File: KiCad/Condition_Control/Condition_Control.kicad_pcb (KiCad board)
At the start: 2 copper layers, 100 x 100 mm, 16 parts, among them J1 Conn_01x04_Socket, J2 Conn_01x03_Socket, J3 Conn_01x02_Socket, J4 Conn_01x02_Socket, U1 74LS04, U2 74LS138, U3 74LS04, U4 74LS08, U5 74LS32, U6 74LS08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

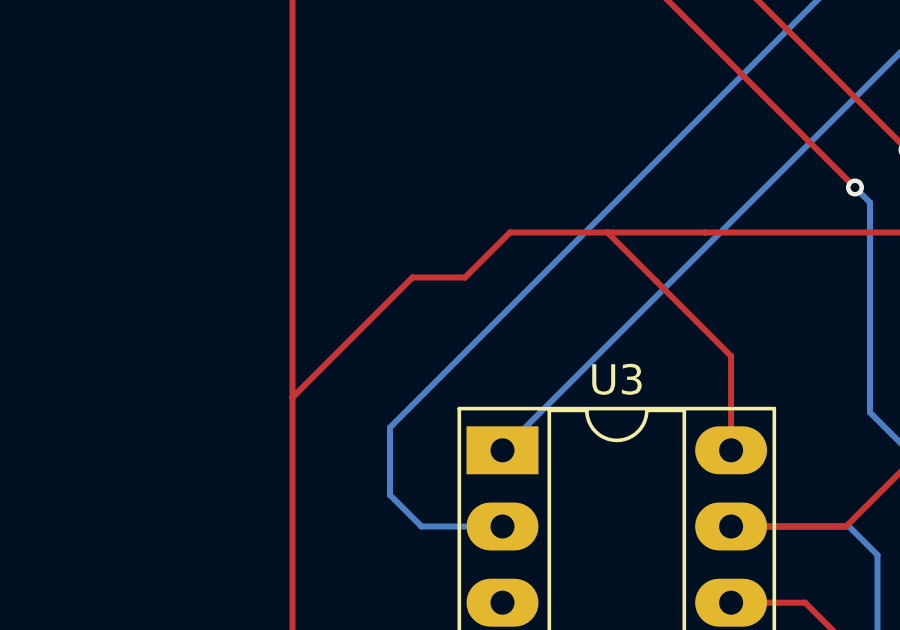
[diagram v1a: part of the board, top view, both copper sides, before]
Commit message: created standarts for PCB's
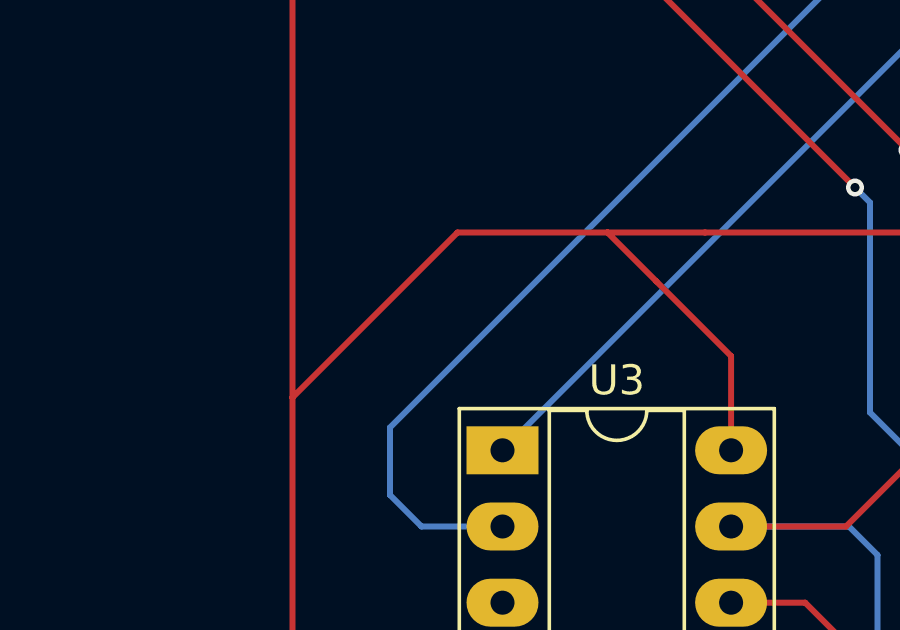
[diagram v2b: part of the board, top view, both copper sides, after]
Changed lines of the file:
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@@
-	)
-	(segment
-		(start 118.75 84)
-		(end 120.25 82.5)
-		(width 0.2)
-		(layer "F.Cu")
-		(net 8)
 	)
 	(segment
@@
 	)
 	(segment
-		(start 120.25 82.5)
-		(end 123.5 82.5)
-		(width 0.2)
-		(layer "F.Cu")
-		(net 8)
-	)
-	(segment
 		(start 161.5 46.5)
 		(end 161.75 46.5)
@@
 	)
 	(segment
-		(start 117 84)
-		(end 118.75 84)
-		(width 0.2)
-		(layer "F.Cu")
-		(net 8)
-	)
-	(segment
 		(start 142.75 46.5)
 		(end 161.5 46.5)
@@
 		(start 184.24 89.76)
 		(end 184.24 87.49)
+		(width 0.2)
+		(layer "F.Cu")
+		(net 8)
+	)
+	(segment
+		(start 113 88)
+		(end 118.5 82.5)
 		(width 0.2)
 		(layer "F.Cu")
@@
 		(start 164.62 86.12)
 		(end 164.62 89.76)
+		(width 0.2)
+		(layer "F.Cu")
+		(net 8)
+	)
+	(segment
+		(start 118.5 82.5)
+		(end 123.5 82.5)
 		(width 0.2)
 		(layer "F.Cu")
@@
 		(width 0.2)
 		(layer "F.Cu")
-		(net 8)
-	)
-	(segment
-		(start 113 88)
-		(end 117 84)
-		(width 0.2)
-		(layer "F.Cu")
